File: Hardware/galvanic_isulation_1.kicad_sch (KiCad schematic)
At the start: 14 parts

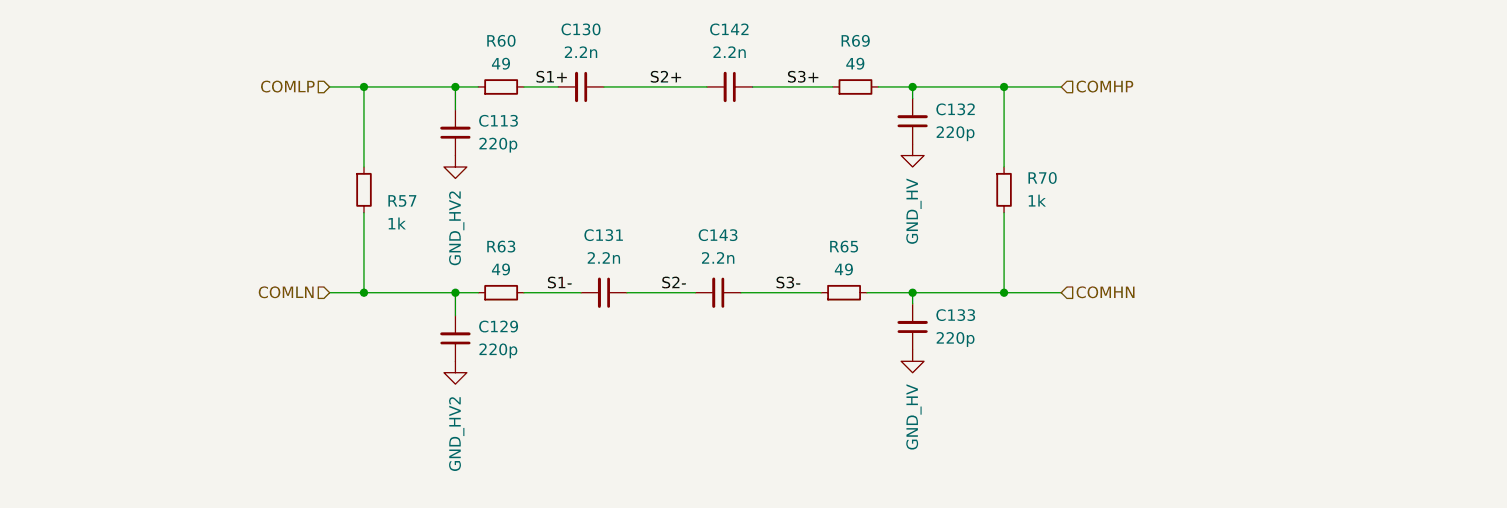
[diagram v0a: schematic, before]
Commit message: Bms plug and play, 2nd iteration with the same pinout
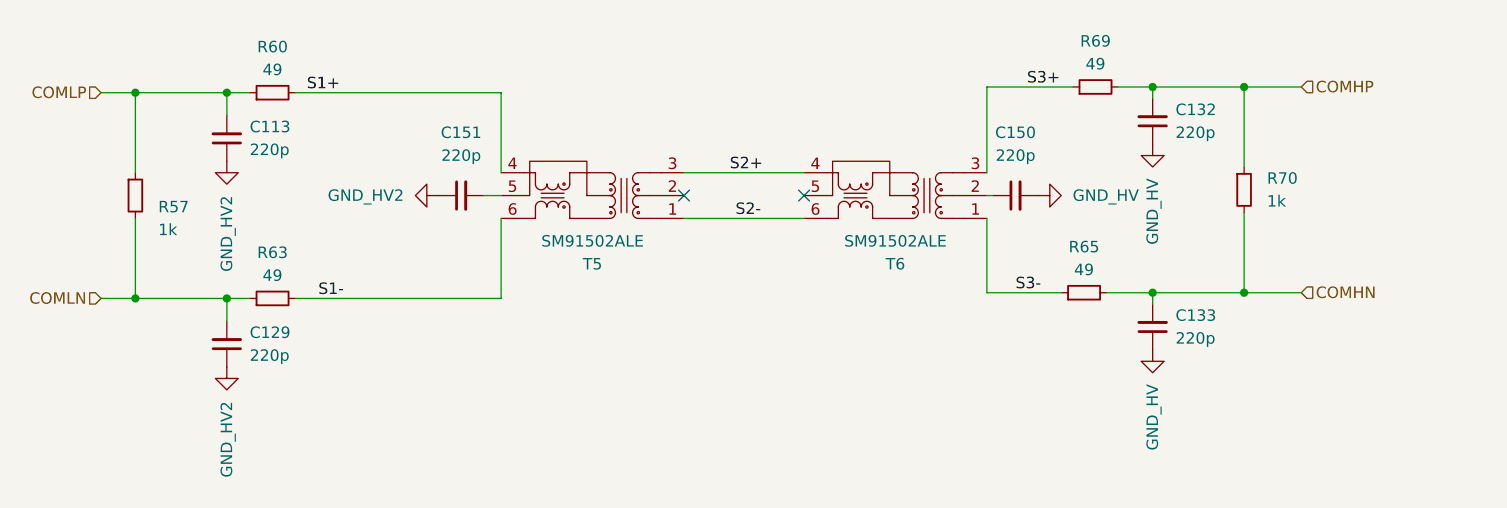
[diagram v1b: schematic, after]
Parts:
- removed C130, C131, C142, C143: 2.2n, footrpint:CAPC5728X280N, symbol Device:C_Small
- added C150, C151: 220p, Capacitor_SMD:C_0603_1608Metric_Pad1.08x0.95mm_HandSolder, symbol Device:C_Small
- added T5, T6: SM91502ALE, footrpint:SOP254P927X572-6N, symbol Samacsys:SM91502ALE
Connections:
- net GND_HV: now also C150.2
- net GND_HV2: now also C151.1
- net S1+: now also T5.4 (SEC_1)
- net S1-: now also T5.6 (SEC_3)
- net S2+: now also T5.3 (PRI_3), T6.4 (SEC_1)
- net S2-: now also T5.1 (PRI_1), T6.6 (SEC_3)
- net S3+: now also T6.3 (PRI_3)
- net S3-: now also T6.1 (PRI_1)
- new net: C151.2, T5.5 (SEC_2)
- new net: C150.1, T6.2 (PRI_2)
- no-connect marks 0 -> 2
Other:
- moved on the sheet: C113, C129, C132, C133, R57, R60, R63, R65, R69, R70

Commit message: New connectors jst_xh for low voltage side of bms
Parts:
- added D38, D39: 13.3V tvs, Package_TO_SOT_SMD:SOT-23, symbol Device:D_TVS_Dual_AAC
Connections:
- net GND_HV: now also D39.3 (common)
- net GND_HV2: now also D38.3 (common)
- net S1+: now also D38.1 (A1)
- net S1-: now also D38.2 (A2)
- net S3+: now also D39.2 (A2)
- net S3-: now also D39.1 (A1)
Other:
- title: (none) -> Battery Management System for a high power gokart battery
- moved on the sheet: C132, C133, R65, R69, R70
